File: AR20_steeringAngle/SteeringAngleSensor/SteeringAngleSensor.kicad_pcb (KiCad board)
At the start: 2 copper layers, 49.5 x 26.7 mm, 4 parts, among them J1 Conn_01x03_Female

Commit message: Added: 90deg JST XH connector
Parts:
- J1: value Conn_01x03_Female -> Conn_01x04_Male; footprint Connector_JST:JST_EH_B3B-EH-A_1x03_P2.50mm_Vertical -> Connector_JST:JST_XH_S4B-XH-A_1x04_P2.50mm_Horizontal
- moved J1 7.11 mm to (143.0, 99.0), turned to 270 degrees
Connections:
- J1 pad 1: /5V -> /GND
- J1 pad 3: /GND -> /5V
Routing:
- net /Out: track 18.6 -> 21.4 mm
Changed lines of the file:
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@@
     (thickness 1.6)
     (drawings 6)
-    (tracks 2)
+    (tracks 5)
     (zones 0)
     (modules 4)
-    (nets 4)
+    (nets 5)
   )
   (page A4)
@@
   )
   (setup
-    (last_trace_width 1.27)
+    (last_trace_width 0.25)
     (user_trace_width 1.27)
     (trace_clearance 0.2)
@@
     (solder_mask_min_width 0.25)
     (aux_axis_origin 0 0)
-    (visible_elements FFFFFF7F)
+    (visible_elements 7FFFFFFF)
     (pcbplotparams
       (layerselection 0x010fc_ffffffff)
@@
   (net 2 /Out)
   (net 3 /5V)
+  (net 4 "Net-(J1-Pad4)")
   (net_class Default "This is the default net class."
     (clearance 0.2)
@@
     (add_net /GND)
     (add_net /Out)
+    (add_net "Net-(J1-Pad4)")
   )
   (module Potentiometer_THT:Potentiometer_Vishay_T73YP_Vertical (layer F.Cu)
@@
     )
   )
-  (module Connector_JST:JST_EH_B3B-EH-A_1x03_P2.50mm_Vertical (layer F.Cu)
-    (at 141.77 106 180)
-    (descr "JST EH series connector, B3B-EH-A (http://www.jst-mfg.com/product/pdf/eng/eEH.pdf), generated with kicad-footprint-generator")
-    (tags "connector JST EH vertical")
-    (fp_text reference J1 (at 2.5 -2.8) (layer F.SilkS)
-      (effects (font (size 1 1) (thickness 0.15)))
-    )
-    (fp_text value Conn_01x03_Female (at 2.5 3.4) (layer F.Fab)
-      (effects (font (size 1 1) (thickness 0.15)))
-    )
-    (fp_text user %R (at 2.5 1.5) (layer F.Fab)
-      (effects (font (size 1 1) (thickness 0.15)))
-    )
-    (fp_line (start -2.91 2.61) (end -0.41 2.61) (layer F.Fab) (width 0.1))
-    (fp_line (start -2.91 0.11) (end -2.91 2.61) (layer F.Fab) (width 0.1))
-    (fp_line (start -2.91 2.61) (end -0.41 2.61) (layer F.SilkS) (width 0.12))
-    (fp_line (start -2.91 0.11) (end -2.91 2.61) (layer F.SilkS) (width 0.12))
-    (fp_line (start 6.61 0.81) (end 6.61 2.31) (layer F.SilkS) (width 0.12))
-    (fp_line (start 7.61 0.81) (end 6.61 0.81) (layer F.SilkS) (width 0.12))
-    (fp_line (start -1.61 0.81) (end -1.61 2.31) (layer F.SilkS) (width 0.12))
-    (fp_line (start -2.61 0.81) (end -1.61 0.81) (layer F.SilkS) (width 0.12))
-    (fp_line (start 7.11 0) (end 7.61 0) (layer F.SilkS) (width 0.12))
-    (fp_line (start 7.11 -1.21) (end 7.11 0) (layer F.SilkS) (width 0.12))
-    (fp_line (start -2.11 -1.21) (end 7.11 -1.21) (layer F.SilkS) (width 0.12))
-    (fp_line (start -2.11 0) (end -2.11 -1.21) (layer F.SilkS) (width 0.12))
-    (fp_line (start -2.61 0) (end -2.11 0) (layer F.SilkS) (width 0.12))
-    (fp_line (start 7.61 -1.71) (end -2.61 -1.71) (layer F.SilkS) (width 0.12))
-    (fp_line (start 7.61 2.31) (end 7.61 -1.71) (layer F.SilkS) (width 0.12))
-    (fp_line (start -2.61 2.31) (end 7.61 2.31) (layer F.SilkS) (width 0.12))
-    (fp_line (start -2.61 -1.71) (end -2.61 2.31) (layer F.SilkS) (width 0.12))
-    (fp_line (start 8 -2.1) (end -3 -2.1) (layer F.CrtYd) (width 0.05))
-    (fp_line (start 8 2.7) (end 8 -2.1) (layer F.CrtYd) (width 0.05))
-    (fp_line (start -3 2.7) (end 8 2.7) (layer F.CrtYd) (width 0.05))
-    (fp_line (start -3 -2.1) (end -3 2.7) (layer F.CrtYd) (width 0.05))
-    (fp_line (start 7.5 -1.6) (end -2.5 -1.6) (layer F.Fab) (width 0.1))
-    (fp_line (start 7.5 2.2) (end 7.5 -1.6) (layer F.Fab) (width 0.1))
-    (fp_line (start -2.5 2.2) (end 7.5 2.2) (layer F.Fab) (width 0.1))
-    (fp_line (start -2.5 -1.6) (end -2.5 2.2) (layer F.Fab) (width 0.1))
-    (pad 3 thru_hole oval (at 5 0 180) (size 1.7 1.95) (drill 0.95) (layers *.Cu *.Mask)
-      (net 1 /GND))
-    (pad 2 thru_hole oval (at 2.5 0 180) (size 1.7 1.95) (drill 0.95) (layers *.Cu *.Mask)
-      (net 2 /Out))
-    (pad 1 thru_hole roundrect (at 0 0 180) (size 1.7 1.95) (drill 0.95) (layers *.Cu *.Mask) (roundrect_rratio 0.147059)
-      (net 3 /5V))
-    (model ${KISYS3DMOD}/Connector_JST.3dshapes/JST_EH_B3B-EH-A_1x03_P2.50mm_Vertical.wrl
-      (at (xyz 0 0 0))
-      (scale (xyz 1 1 1))
-      (rotate (xyz 0 0 0))
-    )
-  )
   (module MountingHole:MountingHole_3.2mm_M3 (layer F.Cu)
     (at 158 90)
@@
     (pad 1 np_thru_hole circle (at 0 0) (size 3.2 3.2) (drill 3.2) (layers *.Cu *.Mask))
   )
+  (module Connector_JST:JST_XH_S4B-XH-A_1x04_P2.50mm_Horizontal (layer F.Cu)
+    (at 143 99 270)
+    (descr "JST XH series connector, S4B-XH-A (http://www.jst-mfg.com/product/pdf/eng/eXH.pdf), generated with kicad-footprint-generator")
+    (tags "connector JST XH horizontal")
+    (fp_text reference J1 (at 3.75 -3.5 90) (layer F.SilkS)
+      (effects (font (size 1 1) (thickness 0.15)))
+    )
+    (fp_text value Conn_01x04_Male (at 3.75 10.4 90) (layer F.Fab)
+      (effects (font (size 1 1) (thickness 0.15)))
+    )
+    (fp_line (start -2.95 -2.8) (end -2.95 9.7) (layer F.CrtYd) (width 0.05))
+    (fp_line (start -2.95 9.7) (end 10.45 9.7) (layer F.CrtYd) (width 0.05))
+    (fp_line (start 10.45 9.7) (end 10.45 -2.8) (layer F.CrtYd) (width 0.05))
+    (fp_line (start 10.45 -2.8) (end -2.95 -2.8) (layer F.CrtYd) (width 0.05))
+    (fp_line (start 3.75 9.31) (end -2.56 9.31) (layer F.SilkS) (width 0.12))
+    (fp_line (start -2.56 9.31) (end -2.56 -2.41) (layer F.SilkS) (width 0.12))
+    (fp_line (start -2.56 -2.41) (end -1.14 -2.41) (layer F.SilkS) (width 0.12))
+    (fp_line (start -1.14 -2.41) (end -1.14 2.09) (layer F.SilkS) (width 0.12))
+    (fp_line (start -1.14 2.09) (end 3.75 2.09) (layer F.SilkS) (width 0.12))
+    (fp_line (start 3.75 9.31) (end 10.06 9.31) (layer F.SilkS) (width 0.12))
+    (fp_line (start 10.06 9.31) (end 10.06 -2.41) (layer F.SilkS) (width 0.12))
+    (fp_line (start 10.06 -2.41) (end 8.64 -2.41) (layer F.SilkS) (width 0.12))
+    (fp_line (start 8.64 -2.41) (end 8.64 2.09) (layer F.SilkS) (width 0.12))
+    (fp_line (start 8.64 2.09) (end 3.75 2.09) (layer F.SilkS) (width 0.12))
+    (fp_line (start 3.75 9.2) (end -2.45 9.2) (layer F.Fab) (width 0.1))
+    (fp_line (start -2.45 9.2) (end -2.45 -2.3) (layer F.Fab) (width 0.1))
+    (fp_line (start -2.45 -2.3) (end -1.25 -2.3) (layer F.Fab) (width 0.1))
+    (fp_line (start -1.25 -2.3) (end -1.25 2.2) (layer F.Fab) (width 0.1))
+    (fp_line (start -1.25 2.2) (end 3.75 2.2) (layer F.Fab) (width 0.1))
+    (fp_line (start 3.75 9.2) (end 9.95 9.2) (layer F.Fab) (width 0.1))
+    (fp_line (start 9.95 9.2) (end 9.95 -2.3) (layer F.Fab) (width 0.1))
+    (fp_line (start 9.95 -2.3) (end 8.75 -2.3) (layer F.Fab) (width 0.1))
+    (fp_line (start 8.75 -2.3) (end 8.75 2.2) (layer F.Fab) (width 0.1))
+    (fp_line (start 8.75 2.2) (end 3.75 2.2) (layer F.Fab) (width 0.1))
+    (fp_line (start -0.25 3.2) (end -0.25 8.7) (layer F.SilkS) (width 0.12))
+    (fp_line (start -0.25 8.7) (end 0.25 8.7) (layer F.SilkS) (width 0.12))
+    (fp_line (start 0.25 8.7) (end 0.25 3.2) (layer F.SilkS) (width 0.12))
+    (fp_line (start 0.25 3.2) (end -0.25 3.2) (layer F.SilkS) (width 0.12))
+    (fp_line (start 2.25 3.2) (end 2.25 8.7) (layer F.SilkS) (width 0.12))
+    (fp_line (start 2.25 8.7) (end 2.75 8.7) (layer F.SilkS) (width 0.12))
+    (fp_line (start 2.75 8.7) (end 2.75 3.2) (layer F.SilkS) (width 0.12))
+    (fp_line (start 2.75 3.2) (end 2.25 3.2) (layer F.SilkS) (width 0.12))
+    (fp_line (start 4.75 3.2) (end 4.75 8.7) (layer F.SilkS) (width 0.12))
+    (fp_line (start 4.75 8.7) (end 5.25 8.7) (layer F.SilkS) (width 0.12))
+    (fp_line (start 5.25 8.7) (end 5.25 3.2) (layer F.SilkS) (width 0.12))
+    (fp_line (start 5.25 3.2) (end 4.75 3.2) (layer F.SilkS) (width 0.12))
+    (fp_line (start 7.25 3.2) (end 7.25 8.7) (layer F.SilkS) (width 0.12))
+    (fp_line (start 7.25 8.7) (end 7.75 8.7) (layer F.SilkS) (width 0.12))
+    (fp_line (start 7.75 8.7) (end 7.75 3.2) (layer F.SilkS) (width 0.12))
+    (fp_line (start 7.75 3.2) (end 7.25 3.2) (layer F.SilkS) (width 0.12))
+    (fp_line (start 0 -1.5) (end -0.3 -2.1) (layer F.SilkS) (width 0.12))
+    (fp_line (start -0.3 -2.1) (end 0.3 -2.1) (layer F.SilkS) (width 0.12))
+    (fp_line (start 0.3 -2.1) (end 0 -1.5) (layer F.SilkS) (width 0.12))
+    (fp_line (start -0.625 2.2) (end 0 1.2) (layer F.Fab) (width 0.1))
+    (fp_line (start 0 1.2) (end 0.625 2.2) (layer F.Fab) (width 0.1))
+    (fp_text user %R (at 3.75 3.45 90) (layer F.Fab)
+      (effects (font (size 1 1) (thickness 0.15)))
+    )
+    (pad 1 thru_hole roundrect (at 0 0 270) (size 1.7 1.95) (drill 0.95) (layers *.Cu *.Mask) (roundrect_rratio 0.147059)
+      (net 1 /GND))
+    (pad 2 thru_hole oval (at 2.5 0 270) (size 1.7 1.95) (drill 0.95) (layers *.Cu *.Mask)
+      (net 2 /Out))
+    (pad 3 thru_hole oval (at 5 0 270) (size 1.7 1.95) (drill 0.95) (layers *.Cu *.Mask)
+      (net 3 /5V))
+    (pad 4 thru_hole oval (at 7.5 0 270) (size 1.7 1.95) (drill 0.95) (layers *.Cu *.Mask)
+      (net 4 "Net-(J1-Pad4)"))
+    (model ${KISYS3DMOD}/Connector_JST.3dshapes/JST_XH_S4B-XH-A_1x04_P2.50mm_Horizontal.wrl
+      (at (xyz 0 0 0))
+      (scale (xyz 1 1 1))
+      (rotate (xyz 0 0 0))
+    )
+  )
   (gr_line (start 114.3 96.52) (end 114.3 83.82) (layer Edge.Cuts) (width 0.05))
   (gr_line (start 133.35 110.49) (end 114.3 96.52) (layer Edge.Cuts) (width 0.05))
@@
   (gr_line (start 163.83 83.82) (end 163.83 96.52) (layer Edge.Cuts) (width 0.05))
   (gr_line (start 114.3 83.82) (end 163.83 83.82) (layer Edge.Cuts) (width 0.05))
-  (segment (start 139.23 105.96) (end 139.27 106) (width 1.27) (layer F.Cu) (net 2))
-  (segment (start 139.23 87.46) (end 139.23 105.96) (width 1.27) (layer F.Cu) (net 2))
+  (segment (start 144.48 101.5) (end 143 101.5) (width 1.27) (layer F.Cu) (net 2))
+  (segment (start 146.1 99.88) (end 144.48 101.5) (width 1.27) (layer F.Cu) (net 2))
+  (segment (start 146.1 90.33) (end 146.1 99.88) (width 1.27) (layer F.Cu) (net 2))
+  (segment (start 139.23 87.46) (end 143.23 87.46) (width 1.27) (layer F.Cu) (net 2))
+  (segment (start 143.23 87.46) (end 146.1 90.33) (width 1.27) (layer F.Cu) (net 2))
   (zone (net 3) (net_name /5V) (layer F.Cu) (hatch edge 0.508)
     (connect_pads (clearance 0.508))

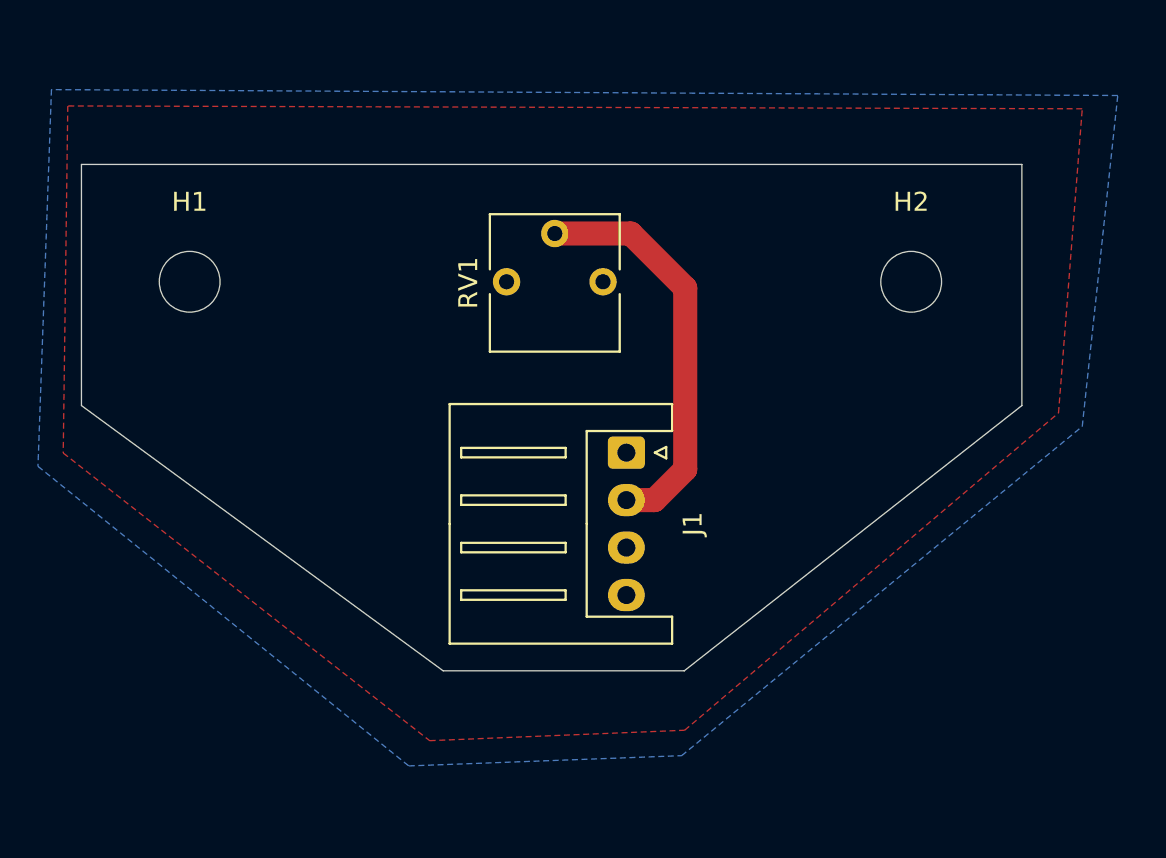
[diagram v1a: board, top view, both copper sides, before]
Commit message: Changed size due to 10x10mm potmeter
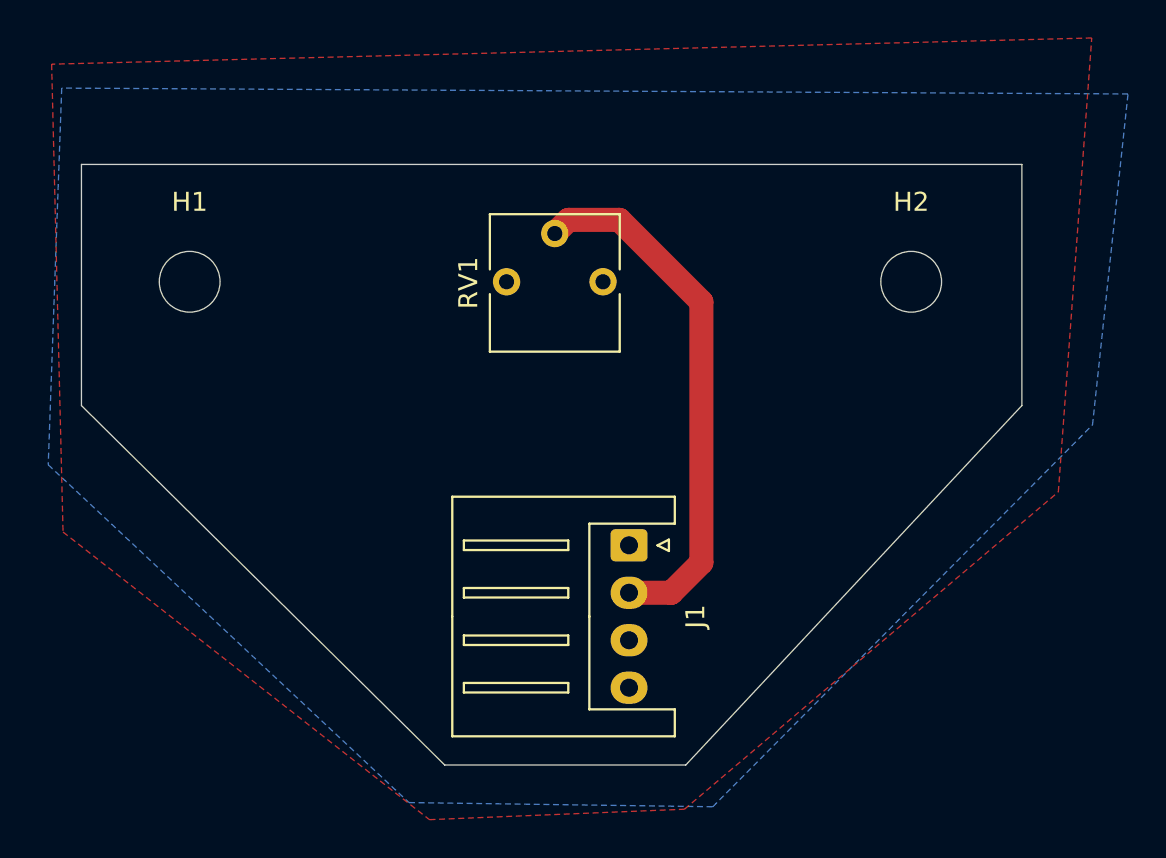
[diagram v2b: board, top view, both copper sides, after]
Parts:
- moved J1 4.88 mm to (143.1, 103.9)
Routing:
- net /Out: track 21.4 -> 28.0 mm
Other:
- board size 49.5 x 26.7 mm -> 49.5 x 31.6 mm
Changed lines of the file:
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@@
     (thickness 1.6)
     (drawings 6)
-    (tracks 5)
+    (tracks 6)
     (zones 0)
     (modules 4)
@@
   )
   (setup
-    (last_trace_width 0.25)
+    (last_trace_width 1.27)
     (user_trace_width 1.27)
     (trace_clearance 0.2)
@@
   )
   (module Connector_JST:JST_XH_S4B-XH-A_1x04_P2.50mm_Horizontal (layer F.Cu)
-    (at 143 99 270)
+    (at 143.14 103.88 270)
     (descr "JST XH series connector, S4B-XH-A (http://www.jst-mfg.com/product/pdf/eng/eXH.pdf), generated with kicad-footprint-generator")
     (tags "connector JST XH horizontal")
@@
   )
   (gr_line (start 114.3 96.52) (end 114.3 83.82) (layer Edge.Cuts) (width 0.05))
-  (gr_line (start 133.35 110.49) (end 114.3 96.52) (layer Edge.Cuts) (width 0.05))
-  (gr_line (start 146.05 110.49) (end 133.35 110.49) (layer Edge.Cuts) (width 0.05))
-  (gr_line (start 163.83 96.52) (end 146.05 110.49) (layer Edge.Cuts) (width 0.05))
+  (gr_line (start 133.43 115.45) (end 114.3 96.52) (layer Edge.Cuts) (width 0.05))
+  (gr_line (start 146.13 115.45) (end 133.43 115.45) (layer Edge.Cuts) (width 0.05))
+  (gr_line (start 163.83 96.52) (end 146.13 115.45) (layer Edge.Cuts) (width 0.05))
   (gr_line (start 163.83 83.82) (end 163.83 96.52) (layer Edge.Cuts) (width 0.05))
   (gr_line (start 114.3 83.82) (end 163.83 83.82) (layer Edge.Cuts) (width 0.05))
-  (segment (start 144.48 101.5) (end 143 101.5) (width 1.27) (layer F.Cu) (net 2))
-  (segment (start 146.1 99.88) (end 144.48 101.5) (width 1.27) (layer F.Cu) (net 2))
-  (segment (start 146.1 90.33) (end 146.1 99.88) (width 1.27) (layer F.Cu) (net 2))
-  (segment (start 139.23 87.46) (end 143.23 87.46) (width 1.27) (layer F.Cu) (net 2))
-  (segment (start 143.23 87.46) (end 146.1 90.33) (width 1.27) (layer F.Cu) (net 2))
+  (segment (start 145.36 106.38) (end 143.14 106.38) (width 1.27) (layer F.Cu) (net 2))
+  (segment (start 146.95 104.79) (end 145.36 106.38) (width 1.27) (layer F.Cu) (net 2))
+  (segment (start 146.95 91.06) (end 146.95 104.79) (width 1.27) (layer F.Cu) (net 2))
+  (segment (start 142.630001 86.740001) (end 146.95 91.06) (width 1.27) (layer F.Cu) (net 2))
+  (segment (start 139.23 87.46) (end 139.949999 86.740001) (width 1.27) (layer F.Cu) (net 2))
+  (segment (start 139.949999 86.740001) (end 142.630001 86.740001) (width 1.27) (layer F.Cu) (net 2))
   (zone (net 3) (net_name /5V) (layer F.Cu) (hatch edge 0.508)
     (connect_pads (clearance 0.508))
@@
     (polygon
       (pts
-        (xy 167.01 80.89) (xy 113.58 80.74) (xy 113.34 99.02) (xy 132.64 114.17) (xy 146.07 113.62)
-        (xy 165.76 96.91)
+        (xy 167.51 77.16) (xy 112.73 78.54) (xy 113.33 103.18) (xy 132.63 118.33) (xy 146.06 117.78)
+        (xy 165.75 101.07)
       )
     )
@@
     (polygon
       (pts
-        (xy 168.88 80.19) (xy 112.72 79.88) (xy 112.01 99.72) (xy 131.54 115.5) (xy 145.91 114.96)
-        (xy 167.01 97.62)
+        (xy 169.42 80.11) (xy 113.26 79.8) (xy 112.55 99.64) (xy 131.55 117.43) (xy 147.55 117.65)
+        (xy 167.55 97.54)
       )
     )

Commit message: Generated Gerber
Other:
- rule via_min_size: 0.4 -> 0.6
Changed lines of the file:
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@@
   )
   (setup
-    (last_trace_width 1.27)
+    (last_trace_width 0.25)
     (user_trace_width 1.27)
     (trace_clearance 0.2)
@@
     (via_size 0.8)
     (via_drill 0.4)
-    (via_min_size 0.4)
+    (via_min_size 0.6)
     (via_min_drill 0.3)
     (uvia_size 0.3)
@@
       (outputformat 1)
       (mirror false)
-      (drillshape 1)
+      (drillshape 0)
       (scaleselection 1)
-      (outputdirectory ""))
+      (outputdirectory "Gerber/"))
   )
   (net 0 "")
